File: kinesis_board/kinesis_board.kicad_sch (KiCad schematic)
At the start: 40 parts, among them J1 RIGHT_13_TOP, J10 LEFT_13_DOWN, J2 RIGHT_13_DOWN, J3 THUMB_RIGHT_SPC_KB600, J4 THUMB_RIGHT_SPC, J5 THUMB_LEFT_BAK, J6 THUMB_LEFT_BAK_KB600, J7 LEFT_1x24, J8 RIGHT_1x24, J9 LEFT_13_TOP

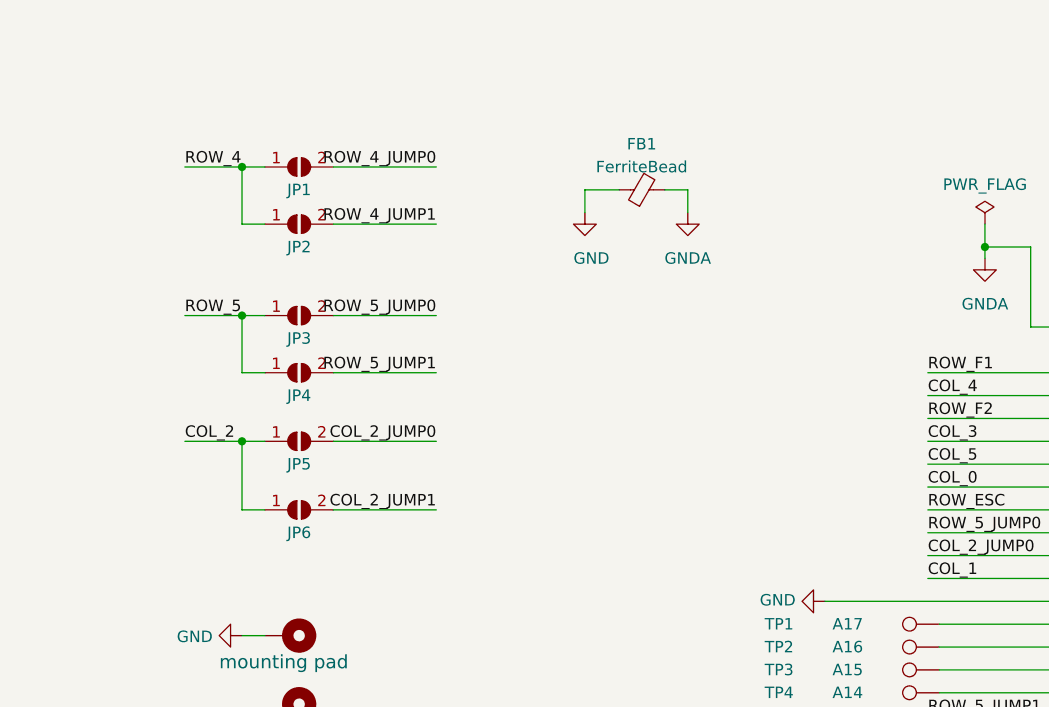
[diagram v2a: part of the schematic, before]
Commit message: finished routing of revision 2.0
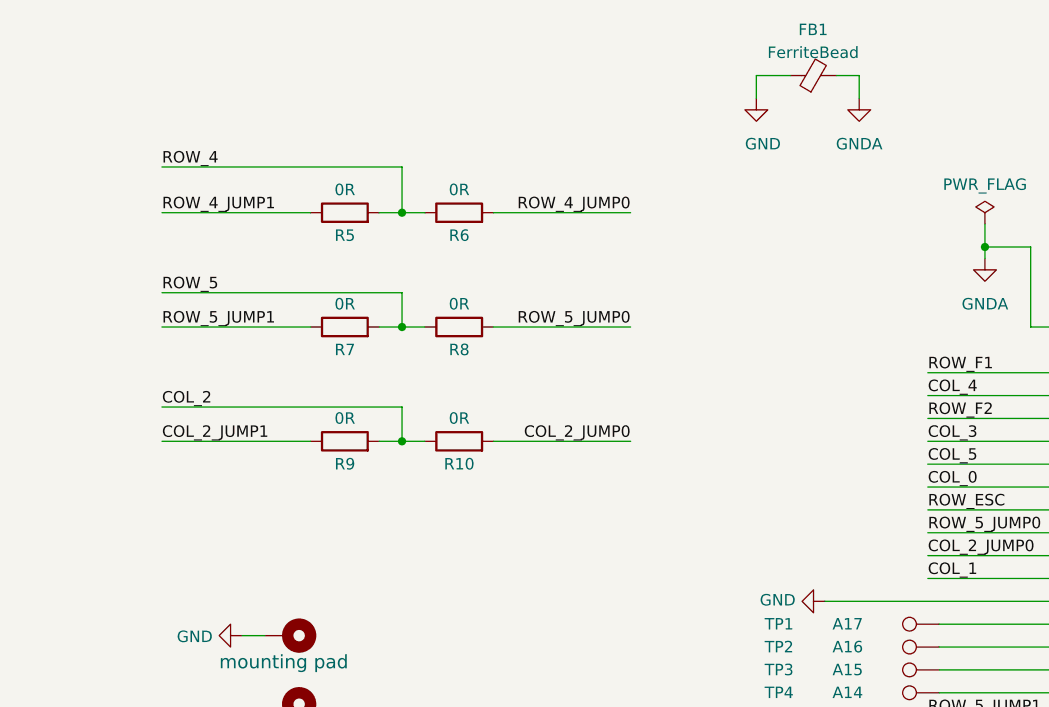
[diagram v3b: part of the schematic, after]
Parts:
- removed JP1, JP2, JP3, JP4, JP5, JP6: SolderJumper_2_Open, Jumper:SolderJumper-2_P1.3mm_Open_RoundedPad1.0x1.5mm, symbol Jumper:SolderJumper_2_Open
- added R10, R5, R6, R7, R8, R9: 0R, Resistor_SMD:R_1206_3216Metric_Pad1.30x1.75mm_HandSolder, symbol Device:R
- R1, R2, R3, R4: footprint Resistor_SMD:R_0805_2012Metric_Pad1.20x1.40mm_HandSolder -> Resistor_SMD:R_1206_3216Metric_Pad1.30x1.75mm_HandSolder
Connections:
- net COL_2: now also R10.1, R9.2
- net COL_2_JUMP0: now also R10.2
- net COL_2_JUMP1: now also R9.1
- net ROW_4: now also R5.2, R6.1
- net ROW_4_JUMP0: now also R6.2
- net ROW_4_JUMP1: now also R5.1
- net ROW_5: now also R7.2, R8.1
- net ROW_5_JUMP0: now also R8.2
- net ROW_5_JUMP1: now also R7.1
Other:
- moved on the sheet: FB1

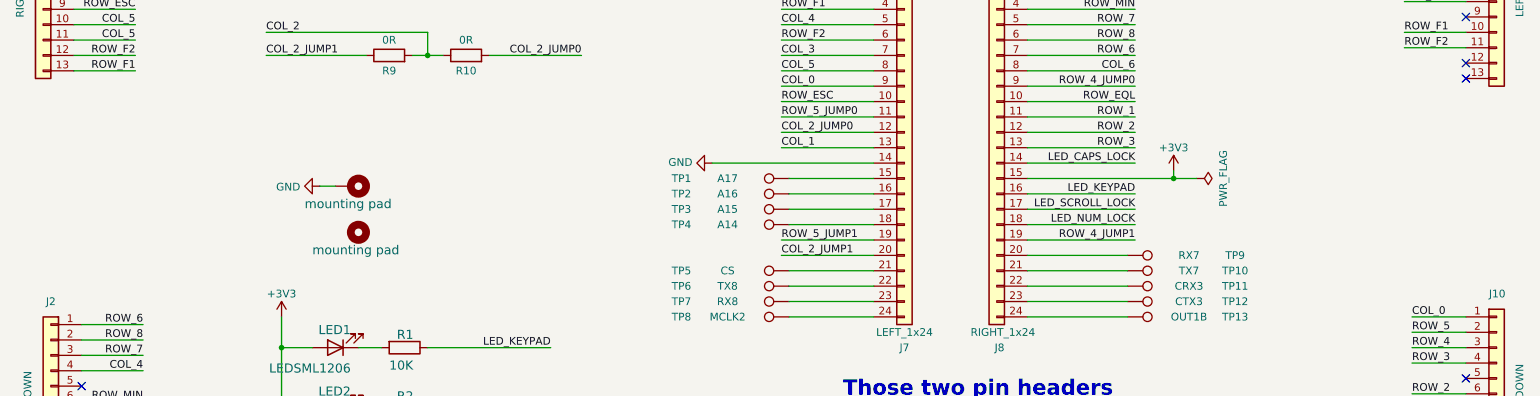
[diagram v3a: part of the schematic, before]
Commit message: added fpc connector to be able to connect new fkeys keypads - not routed yet
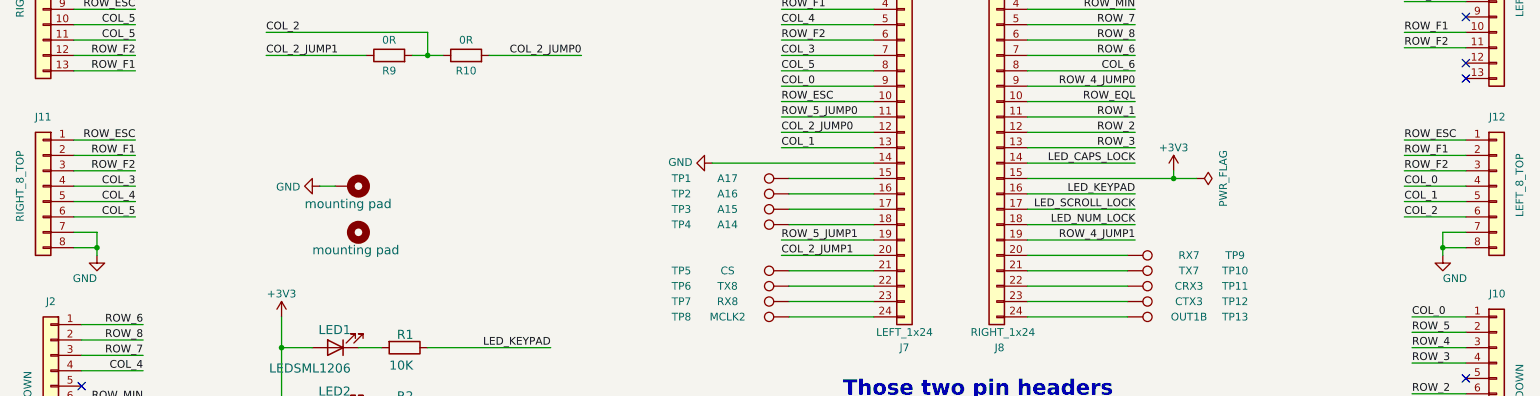
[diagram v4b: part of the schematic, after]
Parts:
- added J11: RIGHT_8_TOP, dodo_conn:84953-6, symbol Connector_Generic:Conn_01x08
- added J12: LEFT_8_TOP, dodo_conn:84953-6, symbol Connector_Generic:Conn_01x08
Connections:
- net COL_0: now also J12.4 (Pin_4)
- net COL_1: now also J12.5 (Pin_5)
- net COL_2: now also J12.6 (Pin_6)
- net COL_3: now also J11.4 (Pin_4)
- net COL_4: now also J11.5 (Pin_5)
- net COL_5: now also J11.6 (Pin_6)
- net GND: now also J11.7 (Pin_7), J11.8 (Pin_8), J12.7 (Pin_7), J12.8 (Pin_8)
- net ROW_ESC: now also J11.1 (Pin_1), J12.1 (Pin_1)
- net ROW_F1: now also J11.2 (Pin_2), J12.2 (Pin_2)
- net ROW_F2: now also J11.3 (Pin_3), J12.3 (Pin_3)

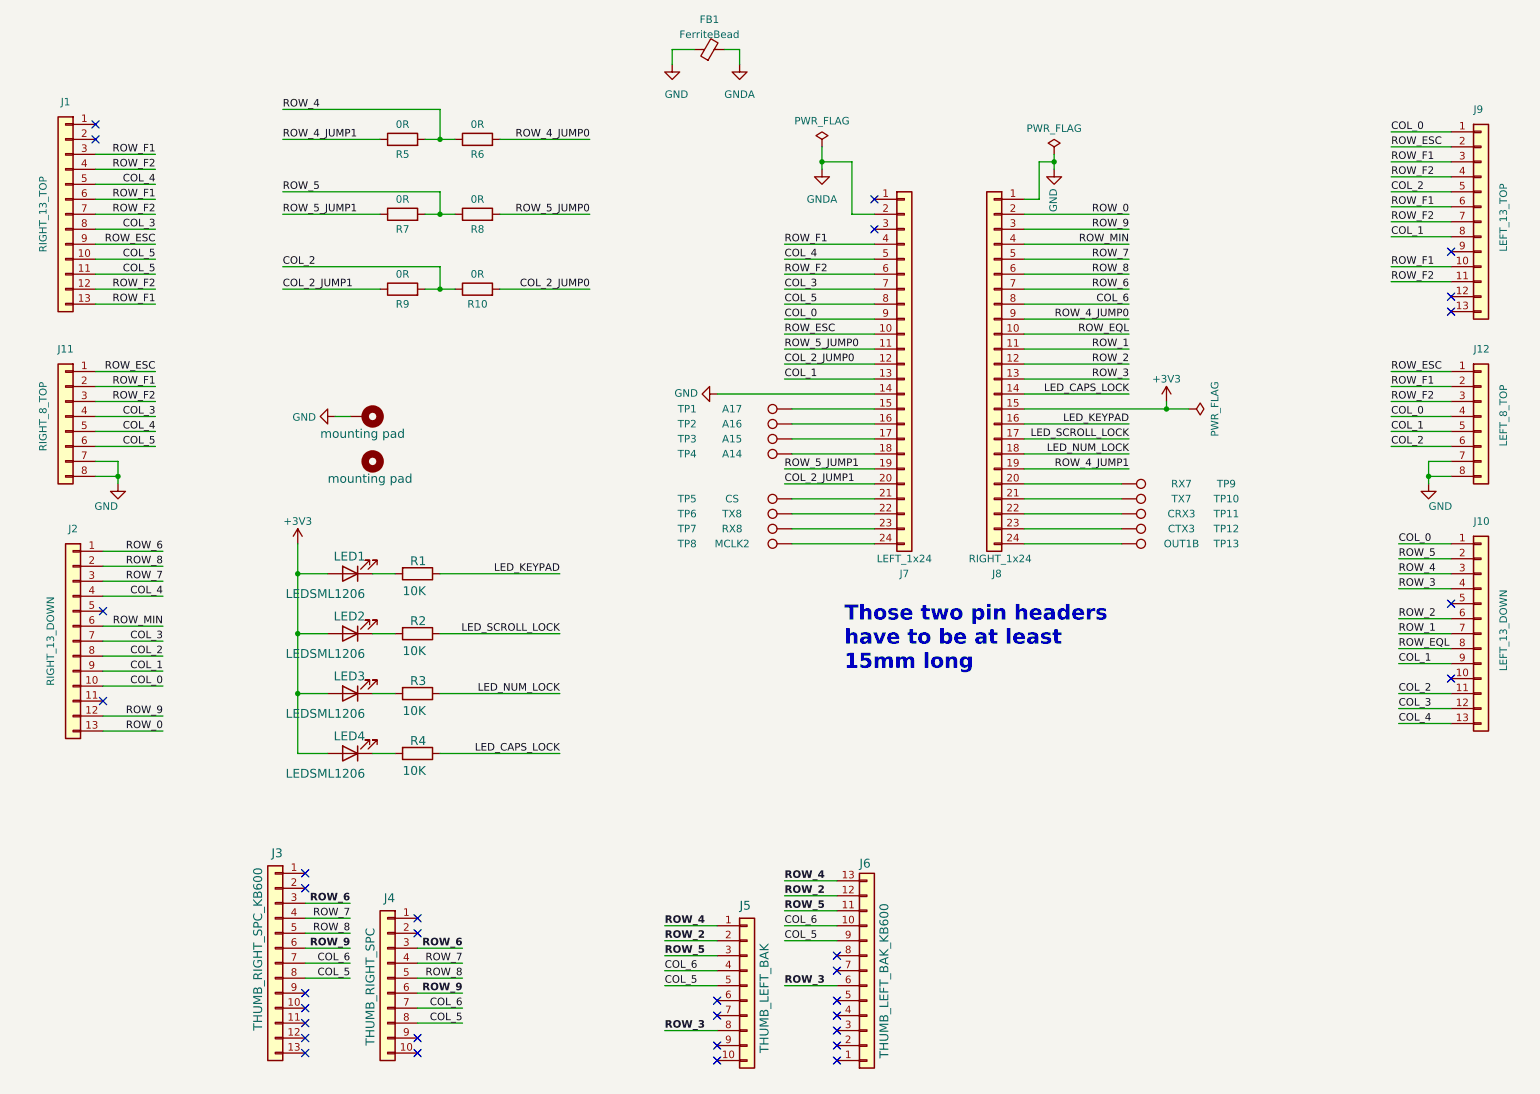
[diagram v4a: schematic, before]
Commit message: updated pcb to use smalle connector and removed the pin headers from the main pcb
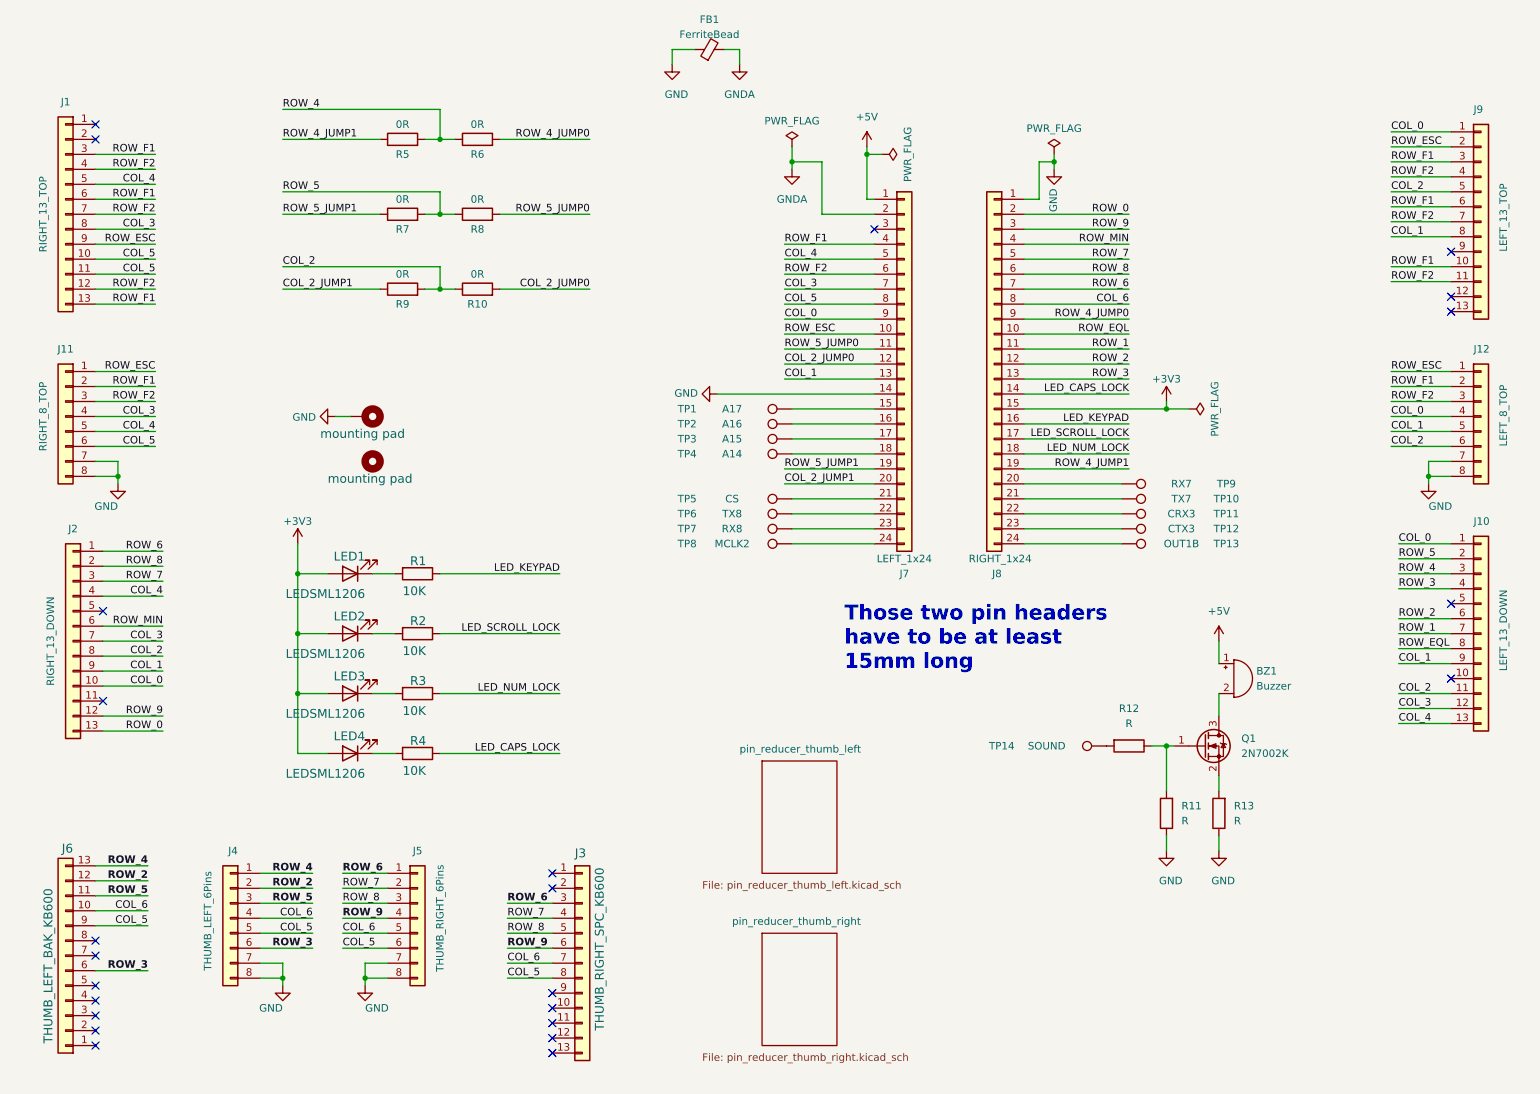
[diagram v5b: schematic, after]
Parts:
- removed J4: THUMB_RIGHT_SPC, Connector_PinHeader_2.54mm:PinHeader_1x10_P2.54mm_Vertical, symbol Connector_Generic:Conn_01x10
- removed J5: THUMB_LEFT_BAK, Connector_PinHeader_2.54mm:PinHeader_1x10_P2.54mm_Vertical, symbol Connector_Generic:Conn_01x10
- added BZ1: Buzzer, Buzzer_Beeper:Buzzer_12x9.5RM7.6, symbol Device:Buzzer
- added J4: THUMB_LEFT_6Pins, dodo_conn:84953-6, symbol Connector_Generic:Conn_01x08
- added J5: THUMB_RIGHT_6Pins, dodo_conn:84953-6, symbol Connector_Generic:Conn_01x08
- added Q1: 2N7002K, Package_TO_SOT_SMD:SOT-23, symbol Transistor_FET:2N7002K
- added R11, R12, R13: R, Resistor_SMD:R_0805_2012Metric_Pad1.20x1.40mm_HandSolder, symbol Device:R
- added TP14: SOUND, TestPoint:TestPoint_Pad_D2.0mm, symbol Connector:TestPoint
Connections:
- net COL_5: now also J4.5 (Pin_5), J5.6 (Pin_6)
- net COL_6: now also J4.4 (Pin_4), J5.5 (Pin_5)
- net GND: now also J4.7 (Pin_7), J4.8 (Pin_8), J5.7 (Pin_7), J5.8 (Pin_8), R11.1, R13.1
- net ROW_2: now also J4.2 (Pin_2)
- net ROW_3: now also J4.6 (Pin_6)
- net ROW_4: now also J4.1 (Pin_1)
- net ROW_5: now also J4.3 (Pin_3)
- net ROW_6: now also J5.1 (Pin_1)
- net ROW_7: now also J5.2 (Pin_2)
- net ROW_8: now also J5.3 (Pin_3)
- net ROW_9: now also J5.4 (Pin_4)
- net +5V: now reaches J7.1 (Pin_1)
- net +5V: now also BZ1.1 (-)
- new net: Q1.1 (G), R11.2, R12.1
- new net: R12.2, TP14.1
- new net: BZ1.2 (+), Q1.3 (D)
- new net: Q1.2 (S), R13.2
- no-connect marks 33 -> 24
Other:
- added sheet pin_reducer_thumb_left (pin_reducer_thumb_left.kicad_sch)
- added sheet pin_reducer_thumb_right (pin_reducer_thumb_right.kicad_sch)
- moved on the sheet: J3, J6

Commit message: removed properties in schematics and updated kicad project version
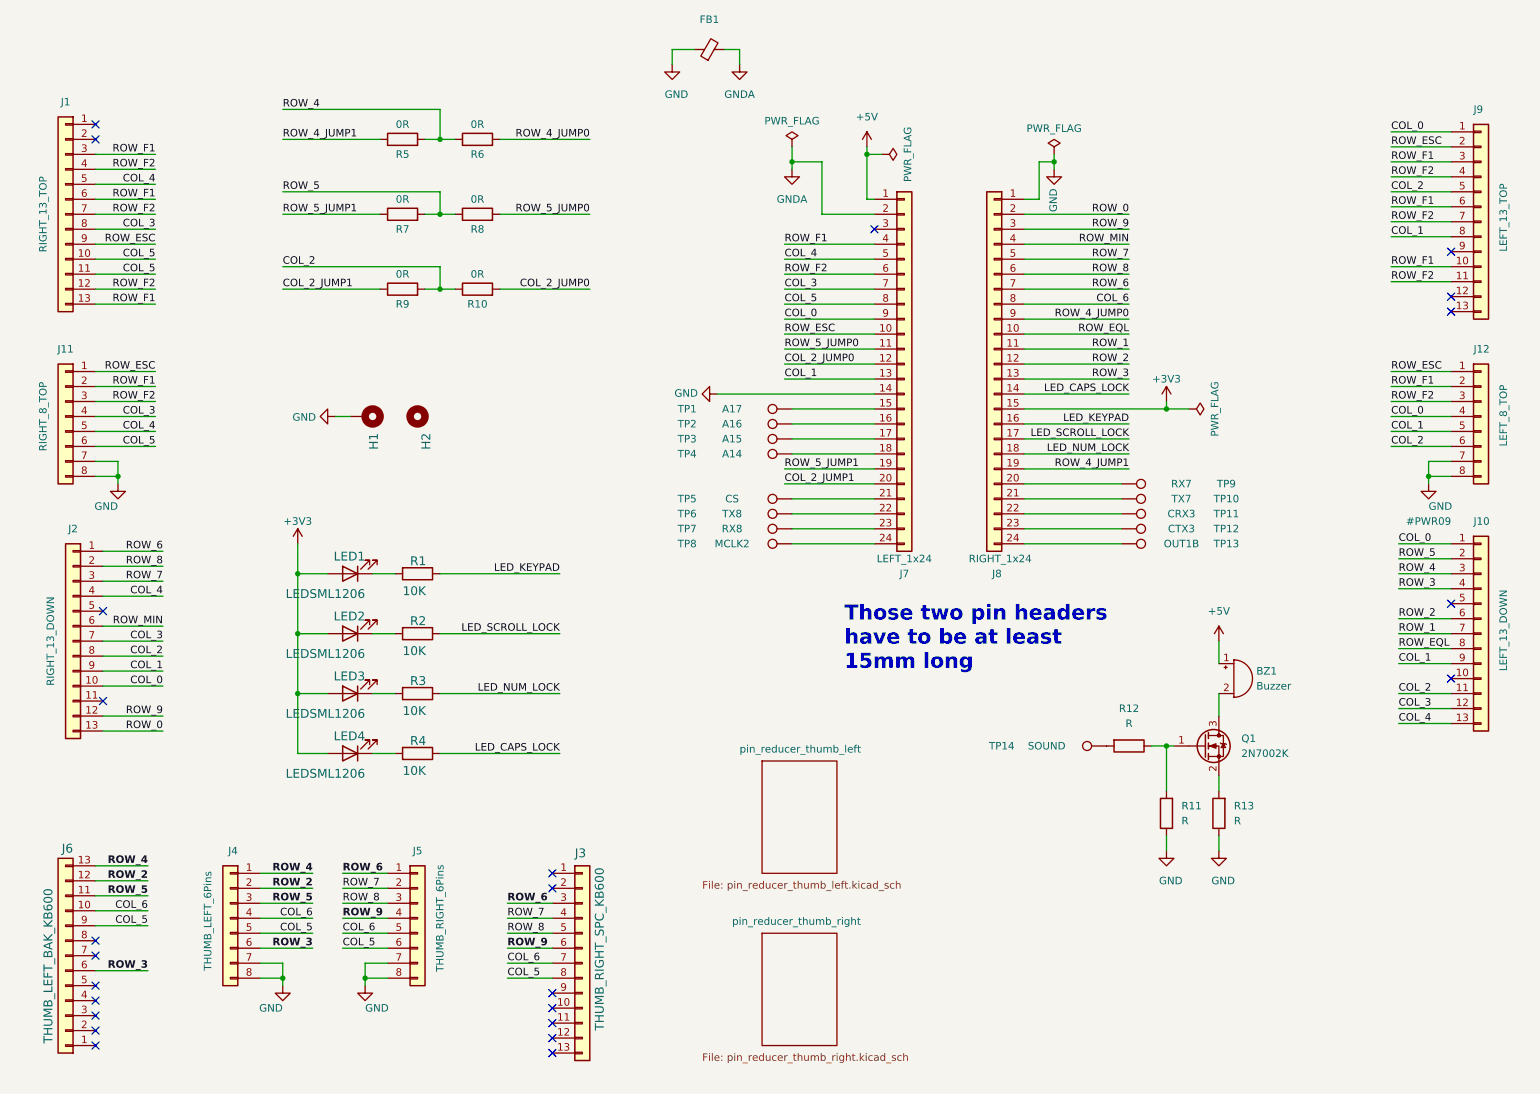
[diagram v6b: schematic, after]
